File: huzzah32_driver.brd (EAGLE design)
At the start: 100 x 80 mm, 9 parts, among them IC1 7805T, J1 1X2-3.5MM, X1 C-GRID-16-70543, X2 C-GRID-12-70543, X3 22-23-2021, X4 22-23-2021

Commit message: I've been working on this for like 6 hours and now it's 4am you expect me to write a commit message? -finished the board
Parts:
- added C3: 330nF, resistor:C050-035X075
- added C4: 100nF, resistor:C050-035X075
- added CN2: (no value), adafruit:DCJACK_2MM_PTH
- added IC2: 7805T, linear:TO220H
- added J2, J3, J4: 1X2-3.5MM, adafruit:1X2-3.5MM
- added JP1, JP2: (no value), pinhead:1X24
- added X10, X7, X8, X9: 22-23-2021, con-molex:22-23-2021
- added X5: C-GRID-16-70543, lumiled_boards:70543-16
- added X6: C-GRID-12-70543, lumiled_boards:70543-12
- moved C1 17.4 mm to (81.0, 24.0), turned to 180 degrees
- moved C2 16.2 mm to (81.0, 17.5), turned to 180 degrees
- moved IC1 12.2 mm to (69.5, 21.5)
- moved X4 10.8 mm to (83.0, 36.0), turned to 90 degrees
- moved X3 9.63 mm to (90.0, 36.0)
- moved X1 9.05 mm to (36.0, 5.50)
- moved X2 9.05 mm to (41.0, 26.0)
- moved J1 3.35 mm to (90.5, 19.5)
- moved CN1 2.90 mm to (98.0, 6.00)
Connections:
- removed net A0_DAC2: X1.12
- removed net A1_DAC1: X1.11
- removed net A2_I34: X1.10
- removed net A3_I39: X1.9
- removed net A4_IO36: X1.8
- removed net A5_IO4: X1.7
- removed net EN: X2.2
- removed net IO12_A11: X2.5
- removed net IO13_A12: X2.4
- removed net IO14_A6: X2.10
- removed net IO15_A8: X2.8
- removed net IO16: X1.3
- removed net IO17: X1.2
- removed net IO21: X1.1
- removed net IO27_A10: X2.6
- removed net IO32_A7: X2.9
- removed net IO33_A9: X2.7
- removed net MISO: X1.4
- removed net MOSI: X1.5
- removed net N$26: X1.14
- removed net RESET: X1.16
- removed net SCK: X1.6
- removed net SCL: X2.11
- removed net SDA: X2.12
- removed net VBAT: X2.1
- new net A0_DAC2_B1: JP1.1, X1.12
- new net A0_DAC2_B2: JP2.1, X5.12
- new net A1_DAC1_B1: JP1.2, X1.11
- new net A1_DAC1_B2: JP2.2, X5.11
- new net A2_I34_B1: JP1.3, X1.10
- new net A2_I34_B2: JP2.3, X5.10
- new net A3_I39_B1: JP1.4, X1.9
- new net A3_I39_B2: JP2.4, X5.9
- new net A4_IO36_B1: JP1.5, X1.8
- new net A4_IO36_B2: JP2.5, X5.8
- new net A5_IO4_B1: JP1.6, X1.7
- new net A5_IO4_B2: JP2.6, X5.7
- new net IO12_A11_B1: JP1.12, X2.5
- new net IO12_A11_B2: JP2.12, X6.5
- new net IO13_A12_B1: JP1.13, X2.4
- new net IO13_A12_B2: JP2.13, X6.4
- new net IO14_A6_B1: JP1.7, X2.10
- new net IO14_A6_B2: JP2.7, X6.10
- new net IO15_A8_B1: JP1.9, X2.8
- new net IO15_A8_B2: JP2.9, X6.8
- new net IO16_B1: JP1.14, X1.3
- new net IO16_B2: JP2.14, X5.3
- new net IO17_B1: JP1.15, X1.2
- new net IO17_B2: JP2.15, X5.2
- new net IO21_B1: JP1.16, X1.1
- new net IO21_B2: JP2.16, X5.1
- new net IO27_A10_B1: JP1.11, X2.6
- new net IO27_A10_B2: JP2.11, X6.6
- new net IO32_A7_B1: JP1.8, X2.9
- new net IO32_A7_B2: JP2.8, X6.9
- new net IO33_A9_B1: JP1.10, X2.7
- new net IO33_A9_B2: JP2.10, X6.7
- new net MISO_B1: JP1.20, X1.4
- new net MISO_B2: JP2.20, X5.4
- new net MOSI_B1: JP1.19, X1.5
- new net MOSI_B2: JP2.19, X5.5
- new net SCK_B1: JP1.21, X1.6
- new net SCK_B2: JP2.21, X5.6
- new net SCL_B1: JP1.17, X2.11
- new net SCL_B2: JP2.17, X6.11
- new net SDA_B1: JP1.18, X2.12
- new net SDA_B2: JP2.18, X6.12
- net +3V3: now also X10.2, X5.15, X9.2
- net +5V: now also C4.1, IC2.3, X6.3, X8.2
- net GND: now also C3.2, C4.2, CN2.GND, CN2.GNDBREAK, IC2.2, J2.1, J3.1, J4.1, JP1.22, JP1.23, JP1.24, JP2.22, JP2.23, JP2.24, X10.1, X5.13, X7.1, X8.1, X9.1
- net V+: now also C3.1, CN2.PWR, IC2.1, J2.2, J3.2, J4.2, X7.2
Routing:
- net +5V: track 0.00 -> 178.3 mm
- net V+: track 0.00 -> 120.1 mm, vias 0 -> 4
- net +3V3: track 0.00 -> 82.2 mm, vias 0 -> 4
- net SCK_B1: track 0.00 -> 52.1 mm
- net A5_IO4_B2: track 0.00 -> 46.0 mm
- net A5_IO4_B1: track 0.00 -> 45.8 mm
- net A0_DAC2_B2: track 0.00 -> 45.4 mm
- net A0_DAC2_B1: track 0.00 -> 45.3 mm
- net A4_IO36_B2: track 0.00 -> 45.0 mm
- net A4_IO36_B1: track 0.00 -> 44.7 mm
- net A3_I39_B1: track 0.00 -> 44.7 mm
- net A1_DAC1_B1: track 0.00 -> 44.7 mm
- net A2_I34_B1: track 0.00 -> 44.7 mm
- net A1_DAC1_B2: track 0.00 -> 44.5 mm
- net A3_I39_B2: track 0.00 -> 44.5 mm
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- added copper zone on layer 1, net GND
- added copper zone on layer 16, net GND
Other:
- board size 100 x 80 mm -> 96.1 x 86.5 mm
- board text added: "+"
- board text added: "12"
- board text added: "13"
- board text added: "14"
- board text added: "15"
- board text added: "16"
- board text added: "17"
- board text added: "18"
- board text added: "19"
- board text added: "21"
- board text added: "21: Digital Only"
- board text added: "22"
- board text added: "23"
- board text added: "27"
- board text added: "3.3V"
- board text added: "32"
- board text added: "33"
- board text added: "34"
- board text added: "36"
- board text added: "39"
- board text added: "4"
- board text added: "5"
- board text added: "5V"
- board text added: "5V Reg"
- board text added: "7805"
- board text added: "A0"
- board text added: "A0-A12: Analog Pins"
- board text added: "A1"
- board text added: "A10"
- board text added: "A11"
- board text added: "A12"
- board text added: "A2"
- board text added: "A3"
- board text added: "A4"
- board text added: "A5"
- board text added: "A6"
- board text added: "A7"
- board text added: "A8"
- board text added: "A9"
- board text added: "DAC1"
- board text added: "DAC1, DAC2: Digital to Analog Pins"
- board text added: "DAC2"
- board text added: "GND"
- board text added: "Huzzah! ESP32"
- board text added: "I2C: SCL, SDA"
- board text added: "MISO"
- board text added: "MOSI"
- board text added: "Pin Descriptions"
- board text added: "RX"
- board text added: "RX, TX: Serial Data"
- board text added: "SCK"
- board text added: "SCL"
- board text added: "SDA"
- board text added: "SJSU 2018"
- board text added: "SPI: MOSI, MISO, SCK"
- board text added: "TX"
- board text added: "VIN"
- board text removed: "ESP32"

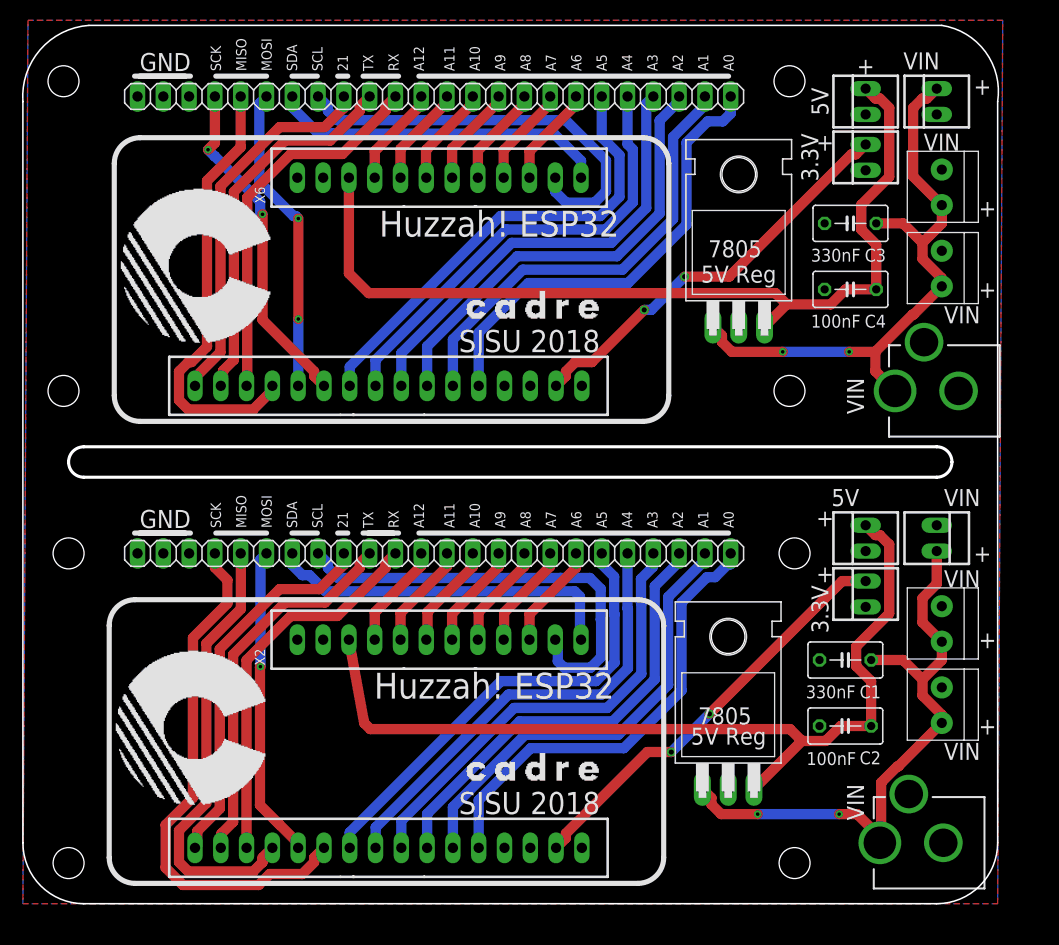
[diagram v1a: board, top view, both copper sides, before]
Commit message: -fixed the issue with the backwards pins
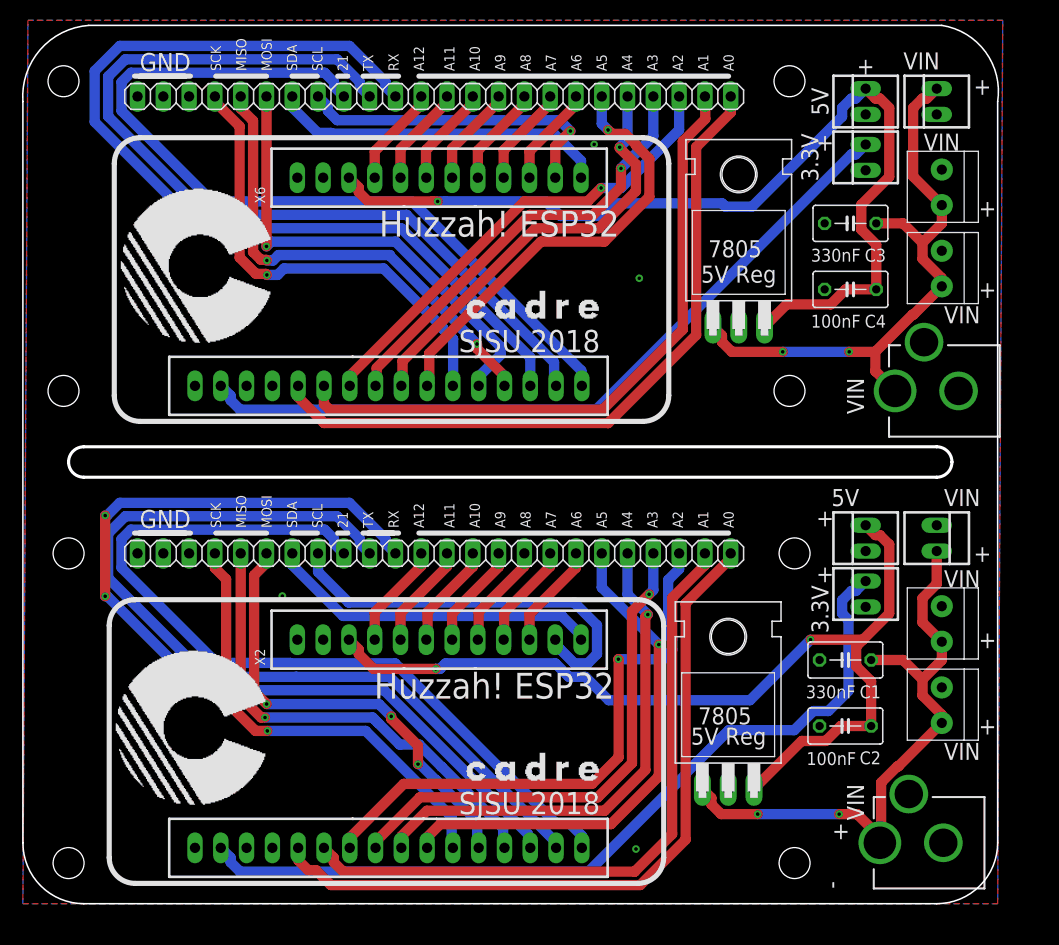
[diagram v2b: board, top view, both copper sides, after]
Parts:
- turned X1 to 180 degrees
- turned X5 to 180 degrees
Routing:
- net +3V3: track 82.2 -> 158.3 mm, vias 4 -> 0
- net IO16_B2: track 37.6 -> 93.3 mm
- net IO16_B1: track 37.8 -> 92.2 mm, vias 0 -> 2
- net IO17_B2: track 37.2 -> 88.5 mm
- net IO17_B1: track 37.4 -> 88.1 mm
- net IO21_B2: track 37.2 -> 83.7 mm
- net IO21_B1: track 37.4 -> 83.8 mm
- net A0_DAC2_B1: track 45.3 -> 72.3 mm
- net A0_DAC2_B2: track 45.4 -> 70.0 mm
- net A1_DAC1_B1: track 44.7 -> 66.0 mm
- net A1_DAC1_B2: track 44.5 -> 64.5 mm
- net MOSI_B2: track 30.5 -> 47.1 mm, vias 2 -> 1
- net MOSI_B1: track 30.8 -> 45.4 mm, vias 1 -> 3
- net SCK_B2: track 33.5 -> 46.4 mm, vias 2 -> 1
- net A2_I34_B1: track 44.7 -> 56.2 mm, vias 0 -> 1
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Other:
- board text added: "-"
